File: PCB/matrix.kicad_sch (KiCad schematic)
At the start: 182 parts, among them SW1 ESC, SW10 F9, SW11 F10, SW12 F11, SW13 F12, SW14 PrSc, SW15 ScLk, SW16 Pause, SW17 `, SW18 1, SW19 2, SW2 F1, SW20 3, SW21 4, SW22 5, SW23 6, SW24 7, SW25 8, SW26 9, SW27 0, SW28 -, SW29 =, SW3 F2, SW30 Backspace, SW31 Ins, SW32 Home, SW33 PgUp, SW34 Tab, SW35 Q, SW36 W, SW37 E, SW38 R, SW39 T, SW4 F3, SW40 Y, SW41 U, SW42 I, SW43 O, SW44 P, SW45 [, SW46 ], SW47 \, SW48 Del, SW49 End, SW5 F4, SW50 PgDn, SW51 CapsLk, SW52 A, SW53 S, SW54 D, SW55 F, SW56 G, SW57 H, SW58 J, SW59 K, SW6 F5, SW60 L, SW61 ;, SW62 ', SW63 Enter, SW64 Shift, SW65 Z, SW66 X, SW67 C, SW68 V, SW69 B, SW7 F6, SW70 N, SW71 M, SW72 ,, SW73 ., SW74 /, SW75 Shift, SW76 Up, SW77 Ctrl, SW78 Win, SW79 Alt, SW8 F7, SW80 Space, SW81 Alt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

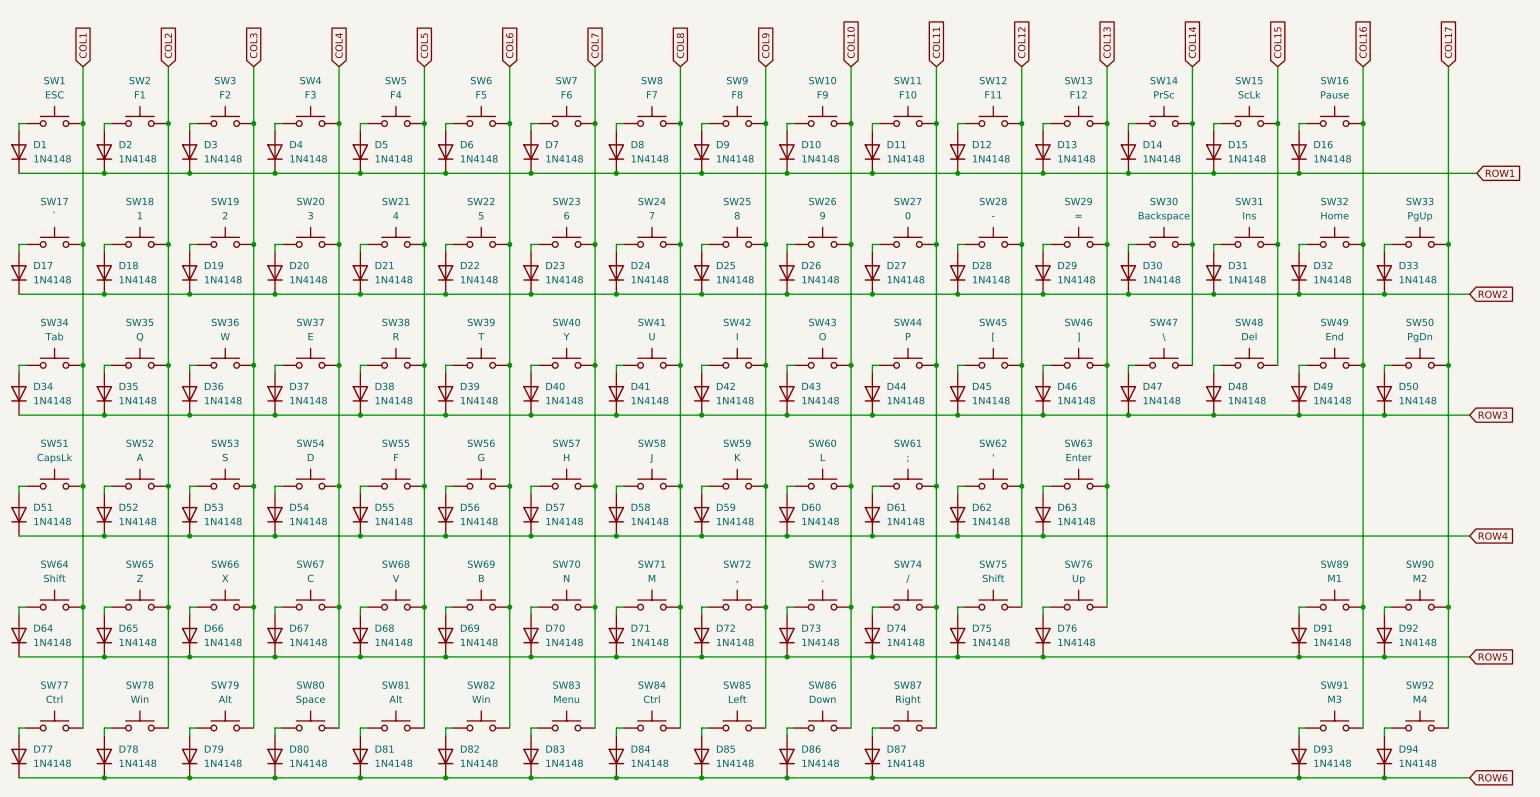
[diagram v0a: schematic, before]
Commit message: change schema to nice! compenents
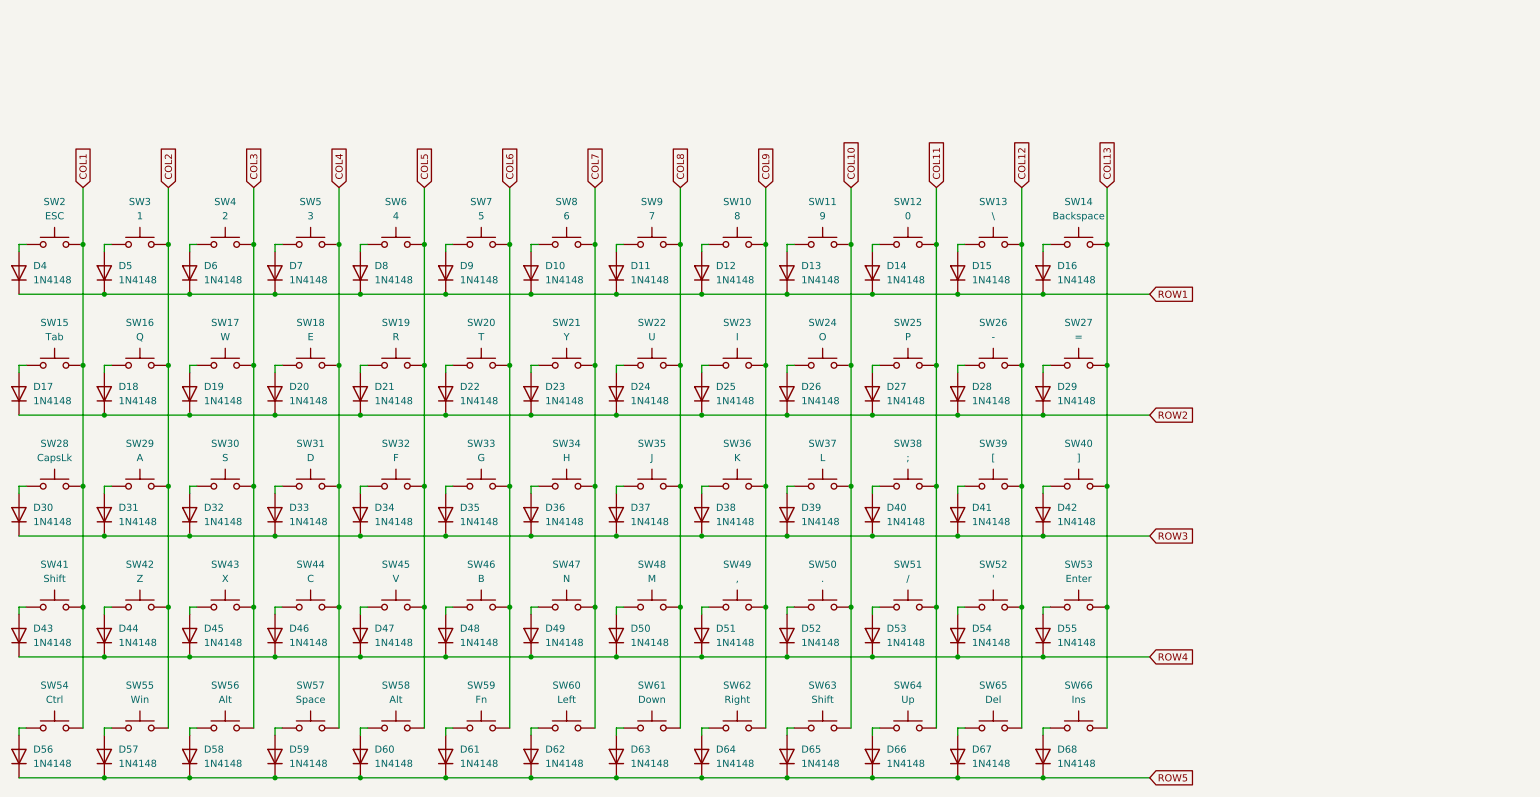
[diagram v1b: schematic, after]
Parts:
- removed D10, D11, D12, D13, D14, D17, D2, D3, D30, D31, D32, D33, D4, D45, D46, D47, D48, D49, D5, D50, D6, D7, D75, D76, D8, D83, D84, D85, D86, D87, D9, D91, D92, D93, D94: 1N4148, Diode_SMD:D_SOD-123, symbol Device:D
- removed SW10: F9, MX_Hotswap:MX-Hotswap-1U, symbol Switch:SW_Push
- removed SW11: F10, MX_Hotswap:MX-Hotswap-1U, symbol Switch:SW_Push
- removed SW12: F11, MX_Hotswap:MX-Hotswap-1U, symbol Switch:SW_Push
- removed SW15: ScLk, MX_Hotswap:MX-Hotswap-1U, symbol Switch:SW_Push
- removed SW16: Pause, MX_Hotswap:MX-Hotswap-1U, symbol Switch:SW_Push
- removed SW17: `, MX_Hotswap:MX-Hotswap-1U, symbol Switch:SW_Push
- removed SW2: F1, MX_Hotswap:MX-Hotswap-1U, symbol Switch:SW_Push
- removed SW28: -, MX_Hotswap:MX-Hotswap-1U, symbol Switch:SW_Push
- removed SW29: =, MX_Hotswap:MX-Hotswap-1U, symbol Switch:SW_Push
- removed SW3: F2, MX_Hotswap:MX-Hotswap-1U, symbol Switch:SW_Push
- removed SW30: Backspace, MX_Hotswap:MX-Hotswap-2U, symbol Switch:SW_Push
- removed SW31: Ins, MX_Hotswap:MX-Hotswap-1U, symbol Switch:SW_Push
- removed SW32: Home, MX_Hotswap:MX-Hotswap-1U, symbol Switch:SW_Push
- removed SW33: PgUp, MX_Hotswap:MX-Hotswap-1U, symbol Switch:SW_Push
- removed SW4: F3, MX_Hotswap:MX-Hotswap-1U, symbol Switch:SW_Push
- removed SW45: [, MX_Hotswap:MX-Hotswap-1U, symbol Switch:SW_Push
- removed SW46: ], MX_Hotswap:MX-Hotswap-1U, symbol Switch:SW_Push
- removed SW47: \, MX_Hotswap:MX-Hotswap-1.5U, symbol Switch:SW_Push
- removed SW48: Del, MX_Hotswap:MX-Hotswap-1U, symbol Switch:SW_Push
- removed SW49: End, MX_Hotswap:MX-Hotswap-1U, symbol Switch:SW_Push
- removed SW5: F4, MX_Hotswap:MX-Hotswap-1U, symbol Switch:SW_Push
- removed SW50: PgDn, MX_Hotswap:MX-Hotswap-1U, symbol Switch:SW_Push
- removed SW6: F5, MX_Hotswap:MX-Hotswap-1U, symbol Switch:SW_Push
- removed SW7: F6, MX_Hotswap:MX-Hotswap-1U, symbol Switch:SW_Push
- removed SW75: Shift, MX_Hotswap:MX-Hotswap-2.75U, symbol Switch:SW_Push
- removed SW76: Up, MX_Hotswap:MX-Hotswap-1U, symbol Switch:SW_Push
- removed SW8: F7, MX_Hotswap:MX-Hotswap-1U, symbol Switch:SW_Push
- removed SW83: Menu, MX_Hotswap:MX-Hotswap-1.25U, symbol Switch:SW_Push
- removed SW84: Ctrl, MX_Hotswap:MX-Hotswap-1.25U, symbol Switch:SW_Push
- removed SW85: Left, MX_Hotswap:MX-Hotswap-1U, symbol Switch:SW_Push
- removed SW86: Down, MX_Hotswap:MX-Hotswap-1U, symbol Switch:SW_Push
- removed SW87: Right, MX_Hotswap:MX-Hotswap-1U, symbol Switch:SW_Push
- removed SW89: M1, MX_Hotswap:MX-Hotswap-1U, symbol Switch:SW_Push
- removed SW9: F8, MX_Hotswap:MX-Hotswap-1U, symbol Switch:SW_Push
- removed SW90: M2, MX_Hotswap:MX-Hotswap-1U, symbol Switch:SW_Push
- removed SW91: M3, MX_Hotswap:MX-Hotswap-1U, symbol Switch:SW_Push
- removed SW92: M4, MX_Hotswap:MX-Hotswap-1U, symbol Switch:SW_Push
- added D41, D42, D54, D55, D64, D65, D66, D67, D68: 1N4148, Diode_SMD:D_SOD-123, symbol Device:D
- added SW26: -, MX_Hotswap:MX-Hotswap-1U, symbol Switch:SW_Push
- added SW27: =, MX_Hotswap:MX-Hotswap-1U, symbol Switch:SW_Push
- added SW39: [, MX_Hotswap:MX-Hotswap-1U, symbol Switch:SW_Push
- added SW40: ], MX_Hotswap:MX-Hotswap-1U, symbol Switch:SW_Push
- added SW52: ', MX_Hotswap:MX-Hotswap-1U, symbol Switch:SW_Push
- added SW53: Enter, MX_Hotswap:MX-Hotswap-2.25U, symbol Switch:SW_Push
- added SW60: Left, MX_Hotswap:MX-Hotswap-1U, symbol Switch:SW_Push
- added SW61: Down, MX_Hotswap:MX-Hotswap-1U, symbol Switch:SW_Push
- added SW64: Up, MX_Hotswap:MX-Hotswap-1U, symbol Switch:SW_Push
- added SW65: Del, MX_Hotswap:MX-Hotswap-1U, symbol Switch:SW_Push
- added SW66: Ins, MX_Hotswap:MX-Hotswap-2.25U, symbol Switch:SW_Push
- SW13: value F12 -> \; footprint MX_Hotswap:MX-Hotswap-1U -> MX_Hotswap:MX-Hotswap-1.5U
- SW14: value PrSc -> Backspace; footprint MX_Hotswap:MX-Hotswap-1U -> MX_Hotswap:MX-Hotswap-2U
- SW59: renamed from SW82; value Win -> Fn
- SW62: value ' -> Right
- SW63: value Enter -> Shift; footprint MX_Hotswap:MX-Hotswap-2.25U -> MX_Hotswap:MX-Hotswap-2.75U
- renumbered D23 to D10, D24 to D11, D25 to D12, D26 to D13, D27 to D14, D34 to D17, D35 to D18, D36 to D19, D37 to D20, D38 to D21, D39 to D22, D40 to D23, D41 to D24, D42 to D25, D43 to D26, D44 to D27, D51 to D30, D52 to D31, D53 to D32, D54 to D33, D55 to D34, D56 to D35, D57 to D36, D58 to D37, D59 to D38, D60 to D39, D1 to D4, D61 to D40, D64 to D43, D65 to D44, D66 to D45, D67 to D46, D68 to D47, D69 to D48, D70 to D49, D18 to D5, D71 to D50, D72 to D51, D73 to D52, D74 to D53, D77 to D56, D78 to D57, D79 to D58, D80 to D59, D19 to D6, D81 to D60, D82 to D61, D20 to D7, D21 to D8, D22 to D9, SW25 to SW10, SW26 to SW11, SW27 to SW12, SW34 to SW15, SW35 to SW16, SW36 to SW17, SW37 to SW18, SW38 to SW19, SW1 to SW2, SW39 to SW20, SW40 to SW21, SW41 to SW22, SW42 to SW23, SW43 to SW24, SW44 to SW25, SW51 to SW28, SW52 to SW29, SW18 to SW3, SW53 to SW30, SW54 to SW31, SW55 to SW32, SW56 to SW33, SW57 to SW34, SW58 to SW35, SW59 to SW36, SW60 to SW37, SW61 to SW38, SW19 to SW4, SW64 to SW41, SW65 to SW42, SW66 to SW43, SW67 to SW44, SW68 to SW45, SW69 to SW46, SW70 to SW47, SW71 to SW48, SW72 to SW49, SW20 to SW5, SW73 to SW50, SW74 to SW51, SW77 to SW54, SW78 to SW55, SW79 to SW56, SW80 to SW57, SW81 to SW58, SW21 to SW6, SW22 to SW7, SW23 to SW8, SW24 to SW9
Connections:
- net COL14 is gone; now on net COL13: SW14.2
- net ROW6 is gone; now on net ROW5: D56.1 (K), D57.1 (K), D58.1 (K), D59.1 (K), D60.1 (K), D61.1 (K)
- net COL10: now also SW63.2
- net COL11: now also SW64.2
- net COL12: now also SW13.2, SW26.2, SW39.2, SW52.2, SW65.2; no longer SW62.2
- net COL13: now also SW27.2, SW40.2, SW53.2, SW66.2; no longer SW13.2, SW63.2
- net COL7: now also SW60.2
- net COL8: now also SW61.2
- net COL9: now also SW62.2
- net ROW1: now also D10.1 (K), D11.1 (K), D12.1 (K), D13.1 (K), D14.1 (K), D5.1 (K), D6.1 (K), D7.1 (K), D8.1 (K), D9.1 (K)
- net ROW2: now also D17.1 (K), D18.1 (K), D19.1 (K), D20.1 (K), D21.1 (K), D22.1 (K), D23.1 (K), D24.1 (K), D25.1 (K), D26.1 (K), D27.1 (K); no longer D10.1 (K), D11.1 (K), D12.1 (K), D13.1 (K), D14.1 (K), D5.1 (K), D6.1 (K), D7.1 (K), D8.1 (K), D9.1 (K)
- net ROW3: now also D30.1 (K), D31.1 (K), D32.1 (K), D33.1 (K), D34.1 (K), D35.1 (K), D36.1 (K), D37.1 (K), D38.1 (K), D39.1 (K), D40.1 (K), D41.1 (K), D42.1 (K); no longer D17.1 (K), D18.1 (K), D19.1 (K), D20.1 (K), D21.1 (K), D22.1 (K), D23.1 (K), D24.1 (K), D25.1 (K), D26.1 (K), D27.1 (K)
- net ROW4: now also D43.1 (K), D44.1 (K), D45.1 (K), D46.1 (K), D47.1 (K), D48.1 (K), D49.1 (K), D50.1 (K), D51.1 (K), D52.1 (K), D53.1 (K), D54.1 (K), D55.1 (K); no longer D30.1 (K), D31.1 (K), D32.1 (K), D33.1 (K), D34.1 (K), D35.1 (K), D36.1 (K), D37.1 (K), D38.1 (K), D39.1 (K), D40.1 (K), D62.1 (K), D63.1 (K)
- net ROW5: now also D62.1 (K), D63.1 (K), D64.1 (K), D65.1 (K), D66.1 (K), D67.1 (K), D68.1 (K); no longer D43.1 (K), D44.1 (K), D45.1 (K), D46.1 (K), D47.1 (K), D48.1 (K), D49.1 (K), D50.1 (K), D51.1 (K), D52.1 (K), D53.1 (K)
- net at D28.2 (A): now also SW26.1
- net at D63.2 (A): now also SW61.1; no longer SW63.1
- net at D62.2 (A): now also SW60.1; no longer SW62.1
- net at D16.2 (A): now also SW14.1
- net at D29.2 (A): now also SW27.1
- net at D15.2 (A): now also SW13.1
- new net: D42.2 (A), SW40.1
- new net: D54.2 (A), SW52.1
- new net: D55.2 (A), SW53.1
- new net: D66.2 (A), SW64.1
- new net: D68.2 (A), SW66.1
- new net: D41.2 (A), SW39.1
- new net: D64.2 (A), SW62.1
- new net: D67.2 (A), SW65.1
- new net: D65.2 (A), SW63.1
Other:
- moved on the sheet: D4, SW2

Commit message: 65% pcb
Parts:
- SW63: footprint MX_Hotswap:MX-Hotswap-2.75U -> MX_Hotswap:MX-Hotswap-1.75U
- SW66: footprint MX_Hotswap:MX-Hotswap-2.25U -> MX_Hotswap:MX-Hotswap-1U
- renumbered D12 to D10, D13 to D11, D14 to D12, D15 to D13, D16 to D14, D17 to D15, D18 to D16, D19 to D17, D20 to D18, D21 to D19, D4 to D2, D22 to D20, D23 to D21, D24 to D22, D25 to D23, D26 to D24, D27 to D25, D28 to D26, D29 to D27, D30 to D28, D31 to D29, D5 to D3, D32 to D30, D33 to D31, D34 to D32, D35 to D33, D36 to D34, D37 to D35, D38 to D36, D39 to D37, D40 to D38, D41 to D39, D6 to D4, D42 to D40, D43 to D41, D44 to D42, D45 to D43, D46 to D44, D47 to D45, D48 to D46, D49 to D47, D50 to D48, D51 to D49, D7 to D5, D52 to D50, D53 to D51, D54 to D52, D55 to D53, D56 to D54, D57 to D55, D58 to D56, D59 to D57, D60 to D58, D61 to D59, D8 to D6, D62 to D60, D63 to D61, D64 to D62, D65 to D63, D66 to D64, D67 to D65, D68 to D66, D9 to D7, D10 to D8, D11 to D9
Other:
- moved on the sheet: D10, D11, D12, D13, D14, D15, D16, D17, D18, D19, D2, D20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
